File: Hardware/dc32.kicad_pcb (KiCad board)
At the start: 2 copper layers, 0 parts

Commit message: Cleaning schematic, ERC, making sure all footprints are in place
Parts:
- added C1: 22uF, Capacitor_SMD:C_0805_2012Metric, F.Cu at (69.3, 117.8)
- added C2: 10uF, Capacitor_SMD:C_0603_1608Metric, F.Cu at (89.6, 54.7)
- added C3: 0.1uF, Capacitor_SMD:C_0603_1608Metric, F.Cu at (89.6, 57.2)
- added C4: 0.1uF, Capacitor_SMD:C_0603_1608Metric, F.Cu at (89.6, 59.7)
- added C5: 0.1uF, Capacitor_SMD:C_0603_1608Metric, F.Cu at (89.6, 62.2)
- added C6: 10uF, Capacitor_SMD:C_0603_1608Metric, F.Cu at (89.6, 64.7)
- added D1: WS2812B, lib_fp:LED_SK6812_4020, F.Cu at (57.2, 55.8)
- added D10: WS2812B, lib_fp:LED_SK6812_4020, F.Cu at (63.2, 63.3)
- added D11: WS2812B, lib_fp:LED_SK6812_4020, F.Cu at (63.2, 67.1)
- added D12: WS2812B, lib_fp:LED_SK6812_4020, F.Cu at (63.2, 70.9)
- added D13: WS2812B, lib_fp:LED_SK6812_4020, F.Cu at (63.2, 74.7)
- added D14: WS2812B, lib_fp:LED_SK6812_4020, F.Cu at (63.2, 78.5)
- added D15: WS2812B, lib_fp:LED_SK6812_4020, F.Cu at (69.3, 55.8)
- added D16: WS2812B, lib_fp:LED_SK6812_4020, F.Cu at (69.3, 59.5)
- added D17: WS2812B, lib_fp:LED_SK6812_4020, F.Cu at (69.3, 63.3)
- added D18: WS2812B, lib_fp:LED_SK6812_4020, F.Cu at (69.3, 67.1)
- added D19: D_Schottky, Diode_SMD:D_SOD-523, F.Cu at (80.2, 117.2)
- added D2: WS2812B, lib_fp:LED_SK6812_4020, F.Cu at (57.2, 59.5)
- added D3: WS2812B, lib_fp:LED_SK6812_4020, F.Cu at (57.2, 63.3)
- added D4: WS2812B, lib_fp:LED_SK6812_4020, F.Cu at (57.2, 67.1)
- added D5: WS2812B, lib_fp:LED_SK6812_4020, F.Cu at (57.2, 70.9)
- added D6: WS2812B, lib_fp:LED_SK6812_4020, F.Cu at (57.2, 74.7)
- added D7: WS2812B, lib_fp:LED_SK6812_4020, F.Cu at (57.2, 78.5)
- added D8: WS2812B, lib_fp:LED_SK6812_4020, F.Cu at (63.2, 55.8)
- added D9: WS2812B, lib_fp:LED_SK6812_4020, F.Cu at (63.2, 59.5)
- added FID1: Fiducial, Fiducial:Fiducial_1mm_Mask2mm, F.Cu at (83.9, 104.9)
- added FID2: Fiducial, Fiducial:Fiducial_1mm_Mask2mm, F.Cu at (83.9, 108.5)
- added FID3: Fiducial, Fiducial:Fiducial_1mm_Mask2mm, F.Cu at (83.9, 112.0)
- added FID4: Fiducial, Fiducial:Fiducial_1mm_Mask2mm, F.Cu at (87.5, 104.9)
- added H1: Top Right, MountingHole:MountingHole_3.2mm_M3_Pad_Via, F.Cu at (58.1, 92.9)
- added H2: Top Left, MountingHole:MountingHole_3.2mm_M3_Pad_Via, F.Cu at (58.1, 100.8)
- added H3: Bottom Right, MountingHole:MountingHole_3.2mm_M3_Pad_Via, F.Cu at (58.1, 108.8)
- added H4: Bottom Left, MountingHole:MountingHole_3.2mm_M3_Pad_Via, F.Cu at (58.1, 116.7)
- added J1: Micro_SD_Card_SPI, lib_fp:MicroSD-Socket-Seeed-320090008, F.Cu at (72.1, 101.4)
- added J2: Conn_01x50, Connector_FFC-FPC:Hirose_FH12-50S-0.5SH_1x50-1MP_P0.50mm_Horizontal, F.Cu at (70.2, 83.5)
- added L1: 1uH, Inductor_SMD:L_1008_2520Metric, F.Cu at (64.6, 118.2)
- added R1: 10R, Resistor_SMD:R_0603_1608Metric, F.Cu at (89.6, 67.2)
- added R2: 33R, Resistor_SMD:R_0603_1608Metric, F.Cu at (89.6, 69.8)
- added R3: 100k, Resistor_SMD:R_0603_1608Metric, F.Cu at (89.6, 72.3)
- added R4: 1M, Resistor_SMD:R_0603_1608Metric, F.Cu at (89.6, 74.8)
- added SW1: SW_SPDT, lib_fp:SW_SPDT_CK-JS102011SAQN, F.Cu at (67.6, 111.5)
- added SW2: Function Select, lib_fp:RotaryEncoder, F.Cu at (79.9, 61.8)
- added TP1: BATT+, TestPoint:TestPoint_Pad_1.5x1.5mm, F.Cu at (87.5, 108.5)
- added TP2: BATT-, TestPoint:TestPoint_Pad_1.5x1.5mm, F.Cu at (87.5, 112.0)
- added TP3: Gain, TestPoint:TestPoint_Pad_1.5x1.5mm, F.Cu at (91.0, 104.9)
- added TP4: SP-, TestPoint:TestPoint_Pad_1.5x1.5mm, F.Cu at (91.0, 108.5)
- added TP5: SP+, TestPoint:TestPoint_Pad_1.5x1.5mm, F.Cu at (91.0, 112.0)
- added U1: SC189ZULTRT, lib_fp:SC189ZULTRT, F.Cu at (80.2, 114.1)
- added U2: INMP4441, lib_fp:MIC_INMP441ACEZ-R7, F.Cu at (76.3, 109.6)
- added U3: Pico, lib_fp:RPi_Pico_SMD, F.Cu at (42.1, 80.0)
- added U4: MAX98357A/B, Package_DFN_QFN:TQFN-16-1EP_3x3mm_P0.5mm_EP1.23x1.23mm, F.Cu at (75.8, 114.9)
- added X1: Badgelife_sao_connector_v169bis, lib_fp:Badgelife-Shitty-v1.69bis-Minimal-Front, F.Cu at (88.9, 92.4)
- added X2: Badgelife_sao_connector_v169bis, lib_fp:Badgelife-Shitty-v1.69bis-Minimal-Front, F.Cu at (88.9, 99.6)
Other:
- board outline added: 88 x 89.5 mm

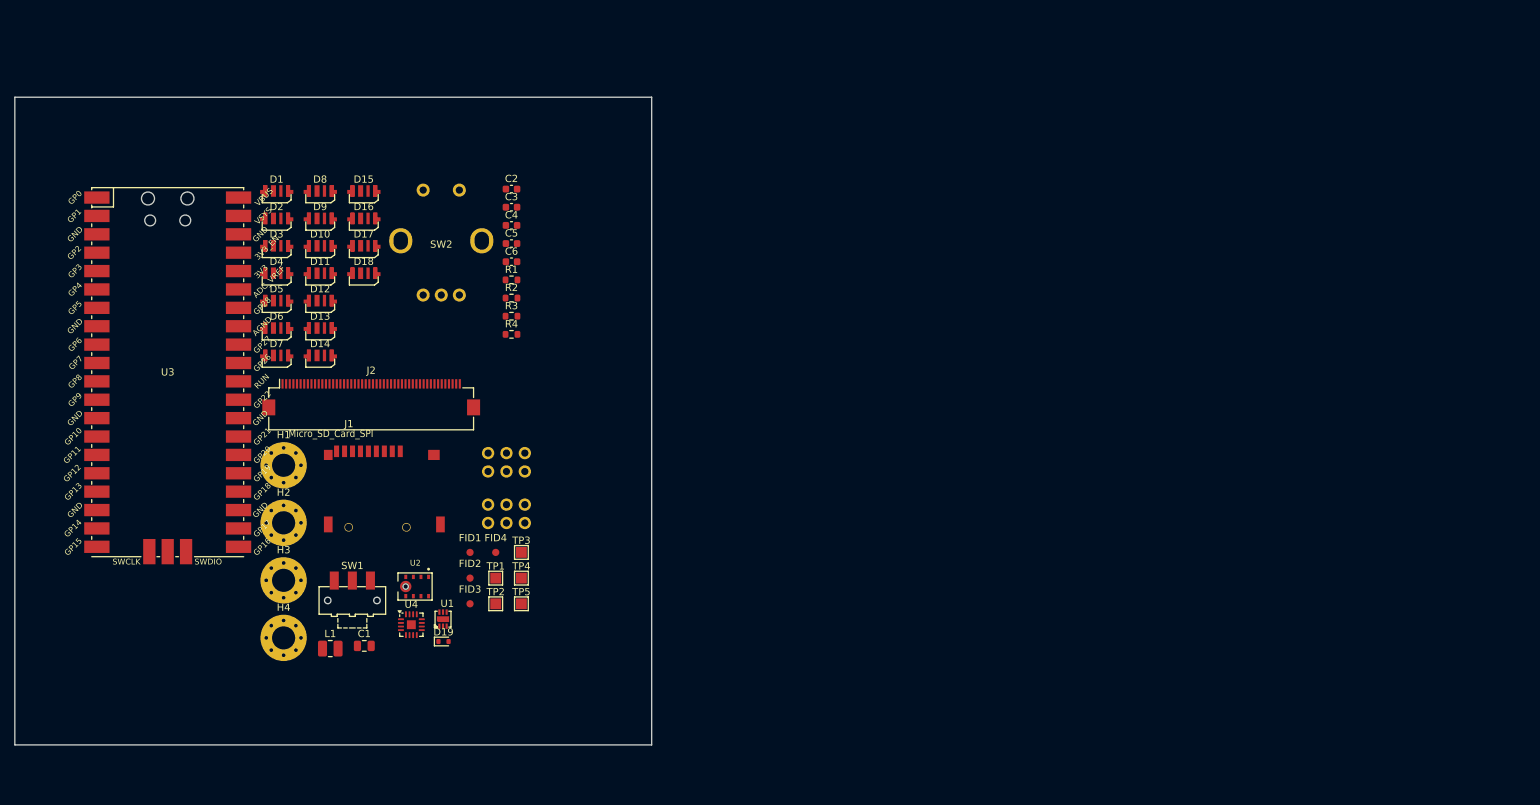
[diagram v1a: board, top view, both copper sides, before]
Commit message: Updated PCBs to rev 1.0 and ordered them
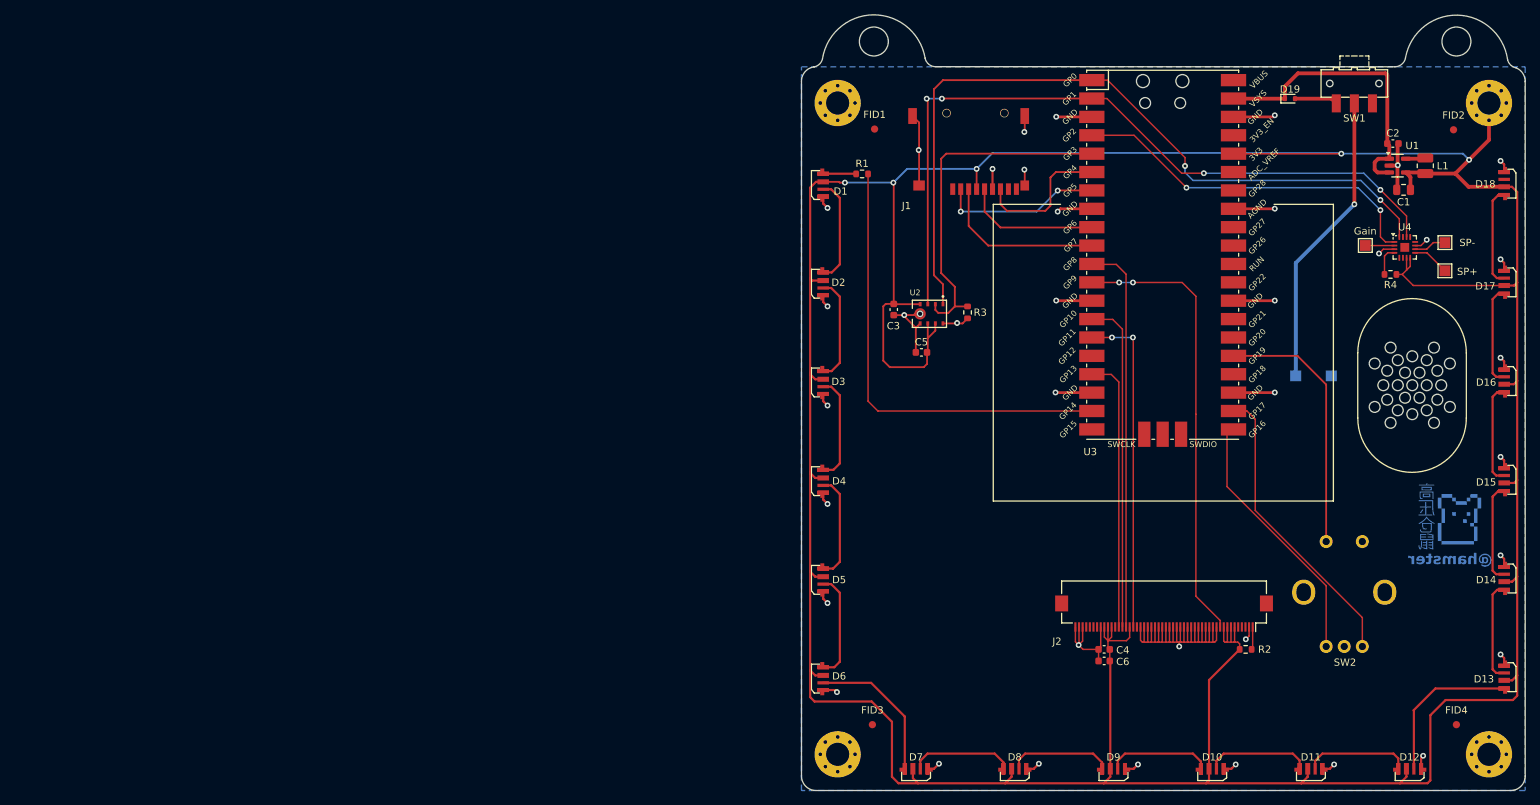
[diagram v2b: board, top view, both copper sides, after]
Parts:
- removed X1, X2: Badgelife_sao_connector_v169bis, lib_fp:Badgelife-Shitty-v1.69bis-Minimal-Front
- added G***: LOGO, lib_fp:hamster, B.Cu at (219.3, 99.9)
- added G***: LOGO, lib_fp:cat-silk, B.Cu at (177.1, 109.5)
- added REF**: Speaker, lib_fp:Speaker, F.Cu at (214.1, 81.8)
- H1, H2, H3, H4, TP1, TP2: moved to B.Cu
- U1: footprint lib_fp:SC189ZULTRT -> Package_TO_SOT_SMD:SOT-23-5
- moved H1 173.9 mm to (224.7, 42.8), turned to 180 degrees
- moved D13 171.1 mm to (227.6, 122.1), turned to 90 degrees
- moved H3 168.3 mm to (224.7, 132.8), turned to 180 degrees
- moved D14 167.1 mm to (227.6, 108.5), turned to 90 degrees
- moved L1 165.4 mm to (215.9, 51.5), turned to -90 degrees
- moved D12 163.8 mm to (213.8, 135.6)
- moved D15 163.1 mm to (227.6, 94.8), turned to 90 degrees
- moved D16 159.8 mm to (227.6, 81.2), turned to 90 degrees
- moved D18 158.9 mm to (227.6, 53.9), turned to 90 degrees
- moved D17 158.4 mm to (227.6, 67.5), turned to 90 degrees
- moved C1 156.8 mm to (212.9, 54.8), turned to 180 degrees
- moved SW1 155.8 mm to (206.1, 40.1), turned to 180 degrees
- moved D11 153.1 mm to (200.1, 135.6)
- moved FID2 149.4 mm to (219.8, 46.5)
- moved U4 146.8 mm to (213.1, 62.8)
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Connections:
- U1 pad 1: (no net) -> VCC
- U1 pad 2: VCC -> GND
- U1 pad 4: Net-(U1-LX) -> +3V3
- U1 pad 5: GND -> Net-(U1-LX)
- U3 pad 19: SDA -> RGB
- U3 pad 20: SCL -> unconnected-(U3-GPIO15-Pad20)
- U3 pad 24: RGB -> unconnected-(U3-GPIO18-Pad24)
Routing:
- net +3V3: track 0.00 -> 557.4 mm, vias 0 -> 5
- net GND: track 0.00 -> 201.2 mm, vias 0 -> 38
- net I2S_BCLK: track 0.00 -> 106.7 mm, vias 0 -> 2
- net I2S_LRCLK: track 0.00 -> 104.4 mm, vias 0 -> 4
- net RGB: track 0.00 -> 63.8 mm
- net LCD_RESET: track 0.00 -> 61.4 mm, vias 0 -> 2
- net LCD_DC: track 0.00 -> 53.2 mm
- net I2S_DIN: track 0.00 -> 49.2 mm, vias 0 -> 2
- net I2S_DOUT: track 0.00 -> 49.0 mm
- net SPI1_SCK: track 0.00 -> 45.1 mm
- net SPI1_MOSI: track 0.00 -> 44.8 mm, vias 0 -> 2
- net ENC1_B: track 0.00 -> 41.9 mm
- net VCC: track 0.00 -> 41.8 mm
- net Net-(SW1-B): track 0.00 -> 41.1 mm, vias 0 -> 1
- net LCD_CS: track 0.00 -> 37.1 mm
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- added copper zone on B.Cu, net GND
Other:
- board size 88 x 89.5 mm -> 100 x 107.2 mm
- board text added: "@hamster"
- board text added: "BATTERY"
- board text added: "DCZIA 2024"
- board text added: "MIC"
- board text added: "REV 1.0"
